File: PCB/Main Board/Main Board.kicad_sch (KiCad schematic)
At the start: 4 parts

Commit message: InAmp Progress
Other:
- sheet Current Amplifier ports: added ACC2.7k, ACC270, ACC27k, ACCen, InAmpx10, InAmpx3, InvAmpx10, InvAmp/2; removed x10, x3, x30/x100
- sheet Signal Source ports: added Bias, In; removed none
- sheet Voltage Amplifier ports: added ACC2.7k, ACC270, ACC27k, ACCen, InAmpx10, InAmpx3, InvAmpx10, InvAmp/2; removed x10, x3, x30/x100
- company: (none) -> Harry and Yuki - EEE3 Instrumentation
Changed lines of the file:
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@@
 	(generator_version "9.0")
 	(paper "A4")
+	(title_block
+		(date "2026-01-15")
+		(rev "Draft")
+		(company "Harry and Yuki - EEE3 Instrumentation")
+		(comment 1 "Work in Progress")
+	)
 	(text "LPOT\n"
 		(exclude_from_sim no)
@@
 	(wire
 		(pts
+			(xy 88.9 38.1) (xy 152.4 38.1)
+		)
+		(stroke
+			(width 0)
+			(type default)
+		)
+	)
+	(wire
+		(pts
 			(xy 177.8 111.76) (xy 190.5 111.76)
 		)
@@
 	(wire
 		(pts
+			(xy 88.9 35.56) (xy 152.4 35.56)
+		)
+		(stroke
+			(width 0)
+			(type default)
+		)
+	)
+	(wire
+		(pts
+			(xy 152.4 76.2) (xy 88.9 76.2)
+		)
+		(stroke
+			(width 0)
+			(type default)
+		)
+	)
+	(wire
+		(pts
 			(xy 215.9 114.3) (xy 228.6 114.3)
 		)
@@
 		(pts
 			(xy 222.25 63.5) (xy 228.6 63.5)
+		)
+		(stroke
+			(width 0)
+			(type default)
+		)
+	)
+	(wire
+		(pts
+			(xy 88.9 114.3) (xy 152.4 114.3)
 		)
 		(stroke
@@
 			)
 		)
+		(pin "Bias" input
+			(at 152.4 35.56 180)
+			(effects
+				(font
+					(size 1.27 1.27)
+				)
+				(justify left)
+			)
+		)
+		(pin "In" input
+			(at 152.4 38.1 180)
+			(effects
+				(font
+					(size 1.27 1.27)
+				)
+				(justify left)
+			)
+		)
 		(instances
 			(project "Main Board"
@@
 			)
 		)
-		(pin "x3" input
+		(pin "ACC2.7k" input
+			(at 152.4 66.04 180)
+			(effects
+				(font
+					(size 1.27 1.27)
+				)
+				(justify left)
+			)
+		)
+		(pin "ACC27k" input
+			(at 152.4 68.58 180)
+			(effects
+				(font
+					(size 1.27 1.27)
+				)
+				(justify left)
+			)
+		)
+		(pin "ACC270" input
+			(at 152.4 71.12 180)
+			(effects
+				(font
+					(size 1.27 1.27)
+				)
+				(justify left)
+			)
+		)
+		(pin "ACCen" input
+			(at 152.4 73.66 180)
+			(effects
+				(font
+					(size 1.27 1.27)
+				)
+				(justify left)
+			)
+		)
+		(pin "InAmpx3" input
+			(at 152.4 78.74 180)
+			(effects
+				(font
+					(size 1.27 1.27)
+				)
+				(justify left)
+			)
+		)
+		(pin "InAmpx10" input
 			(at 152.4 81.28 180)
 			(effects
@@
 			)
 		)
-		(pin "x10" input
+		(pin "InvAmpx10" input
+			(at 152.4 86.36 180)
+			(effects
+				(font
+					(size 1.27 1.27)
+				)
+				(justify left)
+			)
+		)
+		(pin "InvAmp{slash}2" input
 			(at 152.4 83.82 180)
-			(effects
-				(font
-					(size 1.27 1.27)
-				)
-				(justify left)
-			)
-		)
-		(pin "x30{slash}x100" input
-			(at 152.4 86.36 180)
 			(effects
 				(font
@@
 			)
 		)
-		(pin "x3" input
+		(pin "ACC2.7k" input
+			(at 152.4 104.14 180)
+			(effects
+				(font
+					(size 1.27 1.27)
+				)
+				(justify left)
+			)
+		)
+		(pin "ACC27k" input
+			(at 152.4 106.68 180)
+			(effects
+				(font
+					(size 1.27 1.27)
+				)
+				(justify left)
+			)
+		)
+		(pin "ACC270" input
+			(at 152.4 109.22 180)
+			(effects
+				(font
+					(size 1.27 1.27)
+				)
+				(justify left)
+			)
+		)
+		(pin "ACCen" input
+			(at 152.4 111.76 180)
+			(effects
+				(font
+					(size 1.27 1.27)
+				)
+				(justify left)
+			)
+		)
+		(pin "InAmpx3" input
+			(at 152.4 116.84 180)
+			(effects
+				(font
+					(size 1.27 1.27)
+				)
+				(justify left)
+			)
+		)
+		(pin "InAmpx10" input
 			(at 152.4 119.38 180)
 			(effects
@@
 			)
 		)
-		(pin "x10" input
+		(pin "InvAmpx10" input
+			(at 152.4 124.46 180)
+			(effects
+				(font
+					(size 1.27 1.27)
+				)
+				(justify left)
+			)
+		)
+		(pin "InvAmp{slash}2" input
 			(at 152.4 121.92 180)
 			(effects
 				(font
-					(size 1.27 1.27)
-				)
-				(justify left)
-			)
-		)
-		(pin "x30{slash}x100" input
-			(at 152.4 124.46 180)
-			(effects
-				(font

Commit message: ABB, InAmp
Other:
- note added: "Add reference"
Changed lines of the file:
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@@
+		)
+	)
+	(text "Add reference"
+		(exclude_from_sim no)
+		(at 116.84 135.89 0)
+		(effects
+			(font
+				(size 1.27 1.27)
+			)
+			(justify right top)
 		)
 	)
@@
 					(unit 1)
 				)
+			)
+		)
+	)
+	(symbol
+		(lib_id "power:+1V8")
+		(at 124.46 133.35 180)
+		(unit 1)
+		(exclude_from_sim no)
+		(in_bom yes)
+		(on_board yes)
+		(dnp no)
+		(fields_autoplaced yes)
+		(property "Reference" "#PWR0101"
+			(at 124.46 129.54 0)
+			(effects
+				(font
+					(size 1.27 1.27)
+				)
+				(hide yes)
+			)
+		)
+		(property "Value" "+1V8"
+			(at 124.46 138.43 0)
+			(effects
+				(font
+					(size 1.27 1.27)
+				)
+			)
+		)
+		(property "Footprint" ""
+			(at 124.46 133.35 0)
+			(effects
+				(font
+					(size 1.27 1.27)
+				)
+				(hide yes)
+			)
+		)
+		(property "Datasheet" ""
+			(at 124.46 133.35 0)
+			(effects
+				(font
+					(size 1.27 1.27)
+				)
+				(hide yes)
+			)
+		)
+		(property "Description" "Power symbol creates a global label with name \"+1V8\""
+			(at 124.46 133.35 0)
+			(effects
+				(font
+					(size 1.27 1.27)
+				)
+				(hide yes)
+			)
+		)
+		(pin "1"
+		)
+		(instances
+			(project "Main Board"
+				(path "/20aae4b7-3fb8-4924-82e8-1e7a29a313f8"
+					(reference "#PWR0101")
+					(unit 1)
+				)

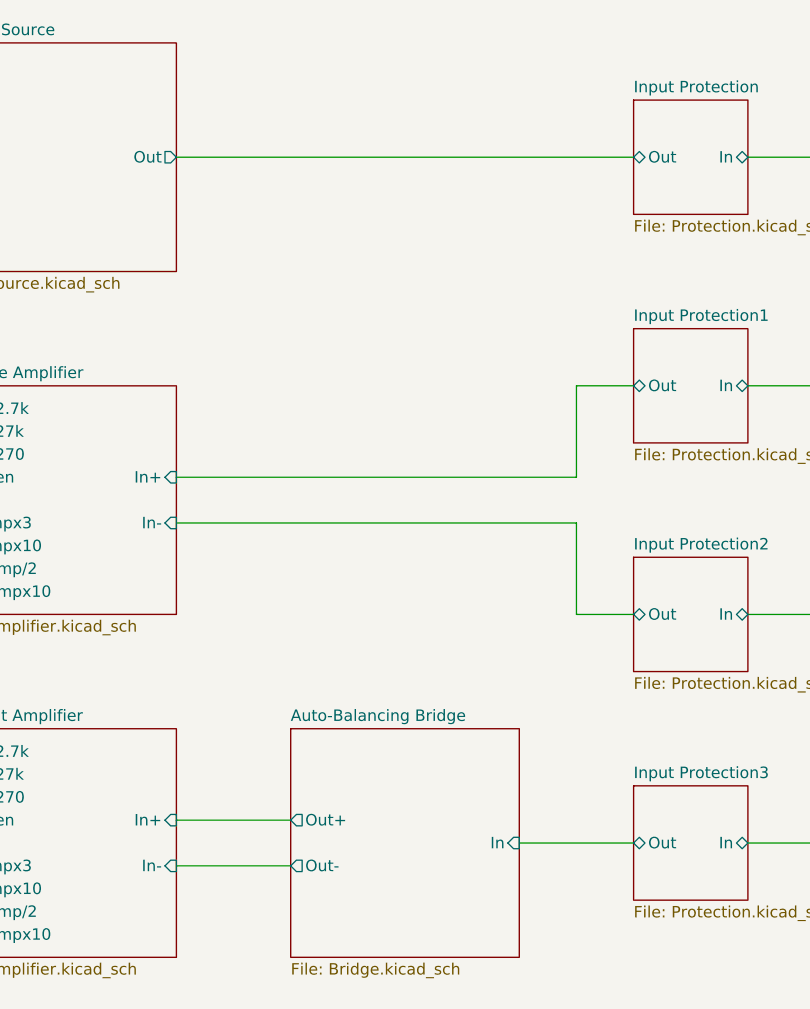
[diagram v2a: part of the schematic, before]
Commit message: Bias sense resistors
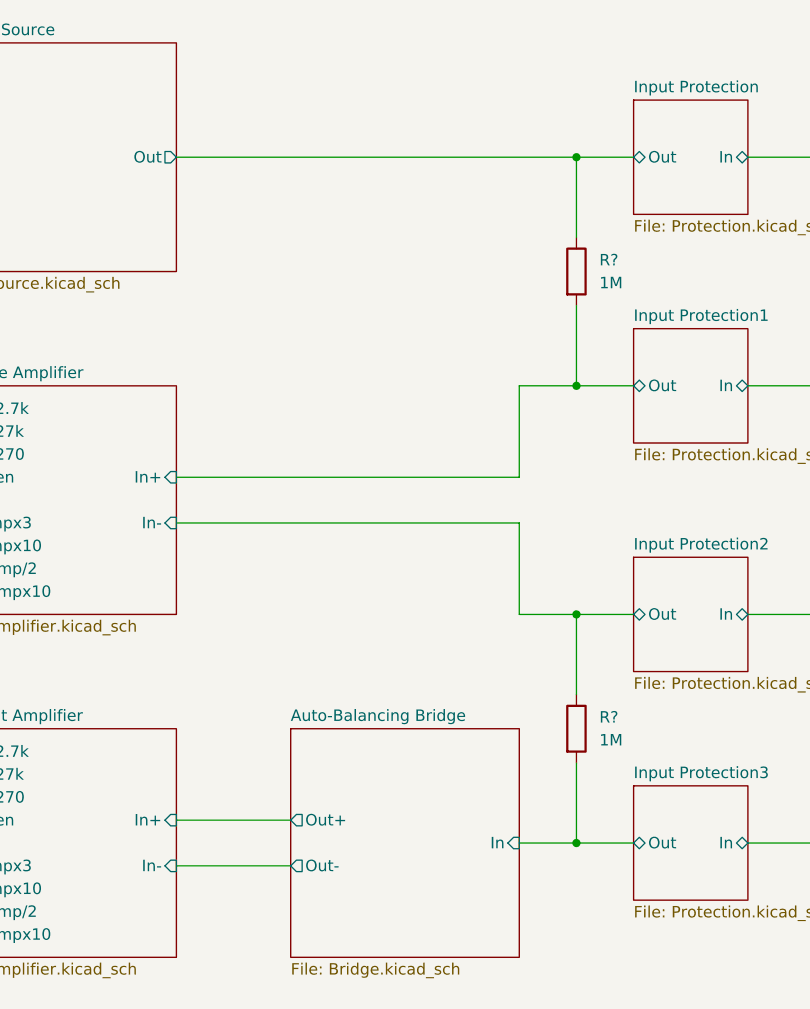
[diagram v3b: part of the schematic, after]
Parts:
- added R? (x2): 1M, symbol Device:R
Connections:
- net Auto-Balancing Bridge/In: now also R?.2
- net Input Protection/Out: now also R?.1
- net Input Protection1/Out: now also R?.2
- net Input Protection2/Out: now also R?.1
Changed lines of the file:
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@@
 		)
 	)
-	(wire
-		(pts
-			(xy 177.8 38.1) (xy 228.6 38.1)
-		)
-		(stroke
-			(width 0)
-			(type default)
-		)
-	)
-	(wire
-		(pts
-			(xy 222.25 73.66) (xy 222.25 63.5)
+	(junction
+		(at 222.25 38.1)
+		(diameter 0)
+		(color 0 0 0 0)
+	)
+	(junction
+		(at 222.25 114.3)
+		(diameter 0)
+		(color 0 0 0 0)
+	)
+	(junction
+		(at 222.25 88.9)
+		(diameter 0)
+		(color 0 0 0 0)
+	)
+	(junction
+		(at 222.25 63.5)
+		(diameter 0)
+		(color 0 0 0 0)
+	)
+	(wire
+		(pts
+			(xy 177.8 38.1) (xy 222.25 38.1)
+		)
+		(stroke
+			(width 0)
+			(type default)
+		)
+	)
+	(wire
+		(pts
+			(xy 215.9 73.66) (xy 215.9 63.5)
 		)
 		(stroke
@@
 	(wire
 		(pts
-			(xy 177.8 78.74) (xy 222.25 78.74)
+			(xy 222.25 88.9) (xy 222.25 97.79)
+		)
+		(stroke
+			(width 0)
+			(type default)
+		)
+	)
+	(wire
+		(pts
+			(xy 222.25 38.1) (xy 222.25 46.99)
+		)
+		(stroke
+			(width 0)
+			(type default)
+		)
+	)
+	(wire
+		(pts
+			(xy 177.8 78.74) (xy 215.9 78.74)
 		)
 		(stroke
@@
 	(wire
 		(pts
-			(xy 215.9 114.3) (xy 228.6 114.3)
-		)
-		(stroke
-			(width 0)
-			(type default)
-		)
-	)
-	(wire
-		(pts
-			(xy 222.25 78.74) (xy 222.25 88.9)
+			(xy 215.9 114.3) (xy 222.25 114.3)
+		)
+		(stroke
+			(width 0)
+			(type default)
+		)
+	)
+	(wire
+		(pts
+			(xy 215.9 78.74) (xy 215.9 88.9)
+		)
+		(stroke
+			(width 0)
+			(type default)
+		)
+	)
+	(wire
+		(pts
+			(xy 222.25 54.61) (xy 222.25 63.5)
 		)
 		(stroke
@@
 	(wire
 		(pts
+			(xy 215.9 88.9) (xy 222.25 88.9)
+		)
+		(stroke
+			(width 0)
+			(type default)
+		)
+	)
+	(wire
+		(pts
 			(xy 177.8 116.84) (xy 190.5 116.84)
 		)
@@
 	(wire
 		(pts
+			(xy 222.25 105.41) (xy 222.25 114.3)
+		)
+		(stroke
+			(width 0)
+			(type default)
+		)
+	)
+	(wire
+		(pts
+			(xy 222.25 114.3) (xy 228.6 114.3)
+		)
+		(stroke
+			(width 0)
+			(type default)
+		)
+	)
+	(wire
+		(pts
+			(xy 222.25 38.1) (xy 228.6 38.1)
+		)
+		(stroke
+			(width 0)
+			(type default)
+		)
+	)
+	(wire
+		(pts
+			(xy 215.9 63.5) (xy 222.25 63.5)
+		)
+		(stroke
+			(width 0)
+			(type default)
+		)
+	)
+	(wire
+		(pts
+			(xy 88.9 114.3) (xy 152.4 114.3)
+		)
+		(stroke
+			(width 0)
+			(type default)
+		)
+	)
+	(wire
+		(pts
+			(xy 241.3 88.9) (xy 248.92 88.9)
+		)
+		(stroke
+			(width 0)
+			(type default)
+		)
+	)
+	(wire
+		(pts
+			(xy 177.8 73.66) (xy 215.9 73.66)
+		)
+		(stroke
+			(width 0)
+			(type default)
+		)
+	)
+	(wire
+		(pts
 			(xy 222.25 63.5) (xy 228.6 63.5)
-		)
-		(stroke
-			(width 0)
-			(type default)
-		)
-	)
-	(wire
-		(pts
-			(xy 88.9 114.3) (xy 152.4 114.3)
-		)
-		(stroke
-			(width 0)
-			(type default)
-		)
-	)
-	(wire
-		(pts
-			(xy 241.3 88.9) (xy 248.92 88.9)
-		)
-		(stroke
-			(width 0)
-			(type default)
-		)
-	)
-	(wire
-		(pts
-			(xy 177.8 73.66) (xy 222.25 73.66)
 		)
 		(stroke
@@
 	)
 	(symbol
+		(lib_id "Device:R")
+		(at 222.25 101.6 0)
+		(unit 1)
+		(exclude_from_sim no)
+		(in_bom yes)
+		(on_board yes)
+		(dnp no)
+		(fields_autoplaced yes)
+		(property "Reference" "R?"
+			(at 224.79 100.3299 0)
+			(effects
+				(font
+					(size 1.27 1.27)
+				)
+				(justify left)
+			)
+		)
+		(property "Value" "1M"
+			(at 224.79 102.8699 0)
+			(effects
+				(font
+					(size 1.27 1.27)
+				)
+				(justify left)
+			)
+		)
+		(property "Footprint" ""
+			(at 220.472 101.6 90)
+			(effects
+				(font
+					(size 1.27 1.27)
+				)
+				(hide yes)
+			)
+		)
+		(property "Datasheet" "~"
+			(at 222.25 101.6 0)
+			(effects
+				(font
+					(size 1.27 1.27)
+				)
+				(hide yes)
+			)
+		)
+		(property "Description" "Resistor"
+			(at 222.25 101.6 0)
+			(effects
+				(font
+					(size 1.27 1.27)
+				)
+				(hide yes)
+			)
+		)
+		(pin "1"
+		)
+		(pin "2"
+		)
+		(instances
+			(project "Main Board"
+				(path "/20aae4b7-3fb8-4924-82e8-1e7a29a313f8"
+					(reference "R?")
+					(unit 1)
+				)
+			)
+		)
+	)
+	(symbol
 		(lib_id "power:+1V8")
 		(at 124.46 133.35 180)
@@
 					(unit 1)
 				)
+			)
+		)
+	)
+	(symbol
+		(lib_id "Device:R")
+		(at 222.25 50.8 0)
+		(unit 1)
+		(exclude_from_sim no)
+		(in_bom yes)
+		(on_board yes)
+		(dnp no)
+		(fields_autoplaced yes)
+		(property "Reference" "R?"
+			(at 224.79 49.5299 0)
+			(effects
+				(font
+					(size 1.27 1.27)
+				)
+				(justify left)
+			)
+		)
+		(property "Value" "1M"
+			(at 224.79 52.0699 0)
+			(effects
+				(font
+					(size 1.27 1.27)
+				)
+				(justify left)
+			)
+		)
+		(property "Footprint" ""
+			(at 220.472 50.8 90)
+			(effects
+				(font
+					(size 1.27 1.27)
+				)
+				(hide yes)
+			)
+		)
+		(property "Datasheet" "~"
+			(at 222.25 50.8 0)
+			(effects
+				(font
+					(size 1.27 1.27)
+				)
+				(hide yes)
+			)
+		)
+		(property "Description" "Resistor"
+			(at 222.25 50.8 0)
+			(effects
+				(font
+					(size 1.27 1.27)
+				)
+				(hide yes)
+			)
+		)
+		(pin "1"
+		)
+		(pin "2"
+		)
+		(instances
+			(project ""
+				(path "/20aae4b7-3fb8-4924-82e8-1e7a29a313f8"
+					(reference "R?")
+					(unit 1)
+				)

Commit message: Paniking further
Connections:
- net Guard_{out}: now reaches J?.2 (Ext)
- net Guard_{out}: now also J?.2 (Ext)
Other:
- added sheet Power (Power.kicad_sch)
- note removed: "Add reference"
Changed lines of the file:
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@@
-		)
-	)
-	(text "Add reference"
-		(exclude_from_sim no)
-		(at 116.84 135.89 0)
-		(effects
-			(font
-				(size 1.27 1.27)
-			)
-			(justify right top)
 		)
 	)
@@
 		)
 	)
+	(label "Guard_{out}"
+		(at 254 119.38 0)
+		(effects
+			(font
+				(size 1.27 1.27)
+			)
+			(justify left top)
+		)
+	)
+	(label "Guard_{out}"
+		(at 254 93.98 0)
+		(effects
+			(font
+				(size 1.27 1.27)
+			)
+			(justify left top)
+		)
+	)
 	(symbol
 		(lib_id "Connector:Conn_Coaxial")
@@
 	)
 	(symbol
-		(lib_id "power:+1V8")
-		(at 124.46 133.35 180)
-		(unit 1)
-		(exclude_from_sim no)
-		(in_bom yes)
-		(on_board yes)
-		(dnp no)
-		(fields_autoplaced yes)
-		(property "Reference" "#PWR0101"
-			(at 124.46 129.54 0)
-			(effects
-				(font
-					(size 1.27 1.27)
-				)
-				(hide yes)
-			)
-		)
-		(property "Value" "+1V8"
-			(at 124.46 138.43 0)
-			(effects
-				(font
-					(size 1.27 1.27)
-				)
-			)
-		)
-		(property "Footprint" ""
-			(at 124.46 133.35 0)
-			(effects
-				(font
-					(size 1.27 1.27)
-				)
-				(hide yes)
-			)
-		)
-		(property "Datasheet" ""
-			(at 124.46 133.35 0)
-			(effects
-				(font
-					(size 1.27 1.27)
-				)
-				(hide yes)
-			)
-		)
-		(property "Description" "Power symbol creates a global label with name \"+1V8\""
-			(at 124.46 133.35 0)
-			(effects
-				(font
-					(size 1.27 1.27)
-				)
-				(hide yes)
-			)
-		)
-		(pin "1"
-		)
-		(instances
-			(project "Main Board"
-				(path "/20aae4b7-3fb8-4924-82e8-1e7a29a313f8"
-					(reference "#PWR0101")
-					(unit 1)
-				)
-			)
-		)
-	)
-	(symbol
 		(lib_id "Connector:Conn_Coaxial")
 		(at 254 63.5 0)
@@
 			(project "Main Board"
 				(path "/20aae4b7-3fb8-4924-82e8-1e7a29a313f8"
-					(page "10")
+					(page "11")
+				)
+			)
+		)
+	)
+	(sheet
+		(at 63.5 139.7)
+		(size 25.4 25.4)
+		(exclude_from_sim no)
+		(in_bom yes)
+		(on_board yes)
+		(dnp no)
+		(fields_autoplaced yes)
+		(stroke
+			(width 0.1524)
+			(type solid)
+		)
+		(fill
+			(color 0 0 0 0.0000)
+		)
+		(property "Sheetname" "Power"
+			(at 63.5 138.9884 0)
+			(effects
+				(font
+					(size 1.27 1.27)
+				)
+				(justify left bottom)
+			)
+		)
+		(property "Sheetfile" "Power.kicad_sch"
+			(at 63.5 165.6846 0)
+			(effects
+				(font
+					(size 1.27 1.27)
+				)
+				(justify left top)
+			)
+		)
+		(instances
+			(project "Main Board"
+				(path "/20aae4b7-3fb8-4924-82e8-1e7a29a313f8"
+					(page "13")
 				)
 			)
@@
 			(project "Main Board"
 				(path "/20aae4b7-3fb8-4924-82e8-1e7a29a313f8"
-					(page "11")
+					(page "12")
 				)
 			)
@@
 			(project "Main Board"
 				(path "/20aae4b7-3fb8-4924-82e8-1e7a29a313f8"
-					(page "8")
+					(page "9")
 				)
 			)
@@
 			(project "Main Board"
 				(path "/20aae4b7-3fb8-4924-82e8-1e7a29a313f8"
-					(page "9")
-				)
-			)
+					(page "10")
+				)
+			)

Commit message: Signal
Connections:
- net Input Protection/Out is gone; now on net Signal Source/Out: R?.1
- net Input Protection1/Out is gone; now on net Voltage Amplifier/In+: R?.2
- net Input Protection2/Out is gone; now on net Voltage Amplifier/In-: R?.1
- net Input Protection3/In is gone; now on net Auto-Balancing Bridge/In: J?.1 (In)
- net Input Protection/In renamed Signal Source/Out
- net Input Protection1/In renamed Voltage Amplifier/In+
- net Input Protection2/In renamed Voltage Amplifier/In-
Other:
- removed sheet Input Protection
- removed sheet Input Protection1
- removed sheet Input Protection2
- removed sheet Input Protection3

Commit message: :anguished:
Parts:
- removed R? (x2): 1M, symbol Device:R
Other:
- sheet Signal Source ports: added x4, /10; removed none
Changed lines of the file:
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@@
-		)
-	)
-	(junction
-		(at 222.25 38.1)
-		(diameter 0)
-		(color 0 0 0 0)
-	)
-	(junction
-		(at 222.25 114.3)
-		(diameter 0)
-		(color 0 0 0 0)
-	)
-	(junction
-		(at 222.25 88.9)
-		(diameter 0)
-		(color 0 0 0 0)
-	)
-	(junction
-		(at 222.25 63.5)
-		(diameter 0)
-		(color 0 0 0 0)
-	)
-	(wire
-		(pts
-			(xy 177.8 38.1) (xy 222.25 38.1)
-		)
-		(stroke
-			(width 0)
-			(type default)
 		)
 	)
@@
 	(wire
 		(pts
-			(xy 222.25 88.9) (xy 222.25 97.79)
-		)
-		(stroke
-			(width 0)
-			(type default)
-		)
-	)
-	(wire
-		(pts
-			(xy 222.25 38.1) (xy 222.25 46.99)
-		)
-		(stroke
-			(width 0)
-			(type default)
-		)
-	)
-	(wire
-		(pts
 			(xy 177.8 78.74) (xy 215.9 78.74)
 		)
@@
 	(wire
 		(pts
-			(xy 222.25 88.9) (xy 248.92 88.9)
+			(xy 215.9 88.9) (xy 248.92 88.9)
 		)
 		(stroke
@@
 	(wire
 		(pts
-			(xy 215.9 114.3) (xy 222.25 114.3)
+			(xy 215.9 114.3) (xy 248.92 114.3)
 		)
 		(stroke
@@
 	(wire
 		(pts
-			(xy 222.25 54.61) (xy 222.25 63.5)
-		)
-		(stroke
-			(width 0)
-			(type default)
-		)
-	)
-	(wire
-		(pts
-			(xy 215.9 88.9) (xy 222.25 88.9)
+			(xy 88.9 45.72) (xy 152.4 45.72)
 		)
 		(stroke
@@
 	(wire
 		(pts
-			(xy 222.25 105.41) (xy 222.25 114.3)
-		)
-		(stroke
-			(width 0)
-			(type default)
-		)
-	)
-	(wire
-		(pts
-			(xy 222.25 114.3) (xy 248.92 114.3)
-		)
-		(stroke
-			(width 0)
-			(type default)
-		)
-	)
-	(wire
-		(pts
-			(xy 222.25 38.1) (xy 248.92 38.1)
-		)
-		(stroke
-			(width 0)
-			(type default)
-		)
-	)
-	(wire
-		(pts
-			(xy 215.9 63.5) (xy 222.25 63.5)
+			(xy 177.8 38.1) (xy 248.92 38.1)
 		)
 		(stroke
@@
 	(wire
 		(pts
-			(xy 222.25 63.5) (xy 248.92 63.5)
+			(xy 215.9 63.5) (xy 248.92 63.5)
+		)
+		(stroke
+			(width 0)
+			(type default)
+		)
+	)
+	(wire
+		(pts
+			(xy 88.9 48.26) (xy 152.4 48.26)
 		)
 		(stroke
@@
 	)
 	(symbol
-		(lib_id "Device:R")
-		(at 222.25 101.6 0)
-		(unit 1)
-		(exclude_from_sim no)
-		(in_bom yes)
-		(on_board yes)
-		(dnp no)
-		(fields_autoplaced yes)
-		(property "Reference" "R?"
-			(at 224.79 100.3299 0)
-			(effects
-				(font
-					(size 1.27 1.27)
-				)
-				(justify left)
-			)
-		)
-		(property "Value" "1M"
-			(at 224.79 102.8699 0)
-			(effects
-				(font
-					(size 1.27 1.27)
-				)
-				(justify left)
-			)
-		)
-		(property "Footprint" ""
-			(at 220.472 101.6 90)
-			(effects
-				(font
-					(size 1.27 1.27)
-				)
-				(hide yes)
-			)
-		)
-		(property "Datasheet" "~"
-			(at 222.25 101.6 0)
-			(effects
-				(font
-					(size 1.27 1.27)
-				)
-				(hide yes)
-			)
-		)
-		(property "Description" "Resistor"
-			(at 222.25 101.6 0)
-			(effects
-				(font
-					(size 1.27 1.27)
-				)
-				(hide yes)
-			)
-		)
-		(pin "1"
-		)
-		(pin "2"
-		)
-		(instances
-			(project "Main Board"
-				(path "/20aae4b7-3fb8-4924-82e8-1e7a29a313f8"
-					(reference "R?")
-					(unit 1)
-				)
-			)
-		)
-	)
-	(symbol
 		(lib_id "Connector:Conn_Coaxial")
 		(at 254 63.5 0)
@@
 				(path "/20aae4b7-3fb8-4924-82e8-1e7a29a313f8"
 					(reference "J?")
-					(unit 1)
-				)
-			)
-		)
-	)
-	(symbol
-		(lib_id "Device:R")
-		(at 222.25 50.8 0)
-		(unit 1)
-		(exclude_from_sim no)
-		(in_bom yes)
-		(on_board yes)
-		(dnp no)
-		(fields_autoplaced yes)
-		(property "Reference" "R?"
-			(at 224.79 49.5299 0)
-			(effects
-				(font
-					(size 1.27 1.27)
-				)
-				(justify left)
-			)
-		)
-		(property "Value" "1M"
-			(at 224.79 52.0699 0)
-			(effects
-				(font
-					(size 1.27 1.27)
-				)
-				(justify left)
-			)
-		)
-		(property "Footprint" ""
-			(at 220.472 50.8 90)
-			(effects
-				(font
-					(size 1.27 1.27)
-				)
-				(hide yes)
-			)
-		)
-		(property "Datasheet" "~"
-			(at 222.25 50.8 0)
-			(effects
-				(font
-					(size 1.27 1.27)
-				)
-				(hide yes)
-			)
-		)
-		(property "Description" "Resistor"
-			(at 222.25 50.8 0)
-			(effects
-				(font
-					(size 1.27 1.27)
-				)
-				(hide yes)
-			)
-		)
-		(pin "1"
-		)
-		(pin "2"
-		)
-		(instances
-			(project ""
-				(path "/20aae4b7-3fb8-4924-82e8-1e7a29a313f8"
-					(reference "R?")
 					(unit 1)
 				)
@@
 			(effects
 				(font
+					(size 1.27 1.27)
+				)
+				(justify left)
+			)
+		)
+		(pin "x4" input
+			(at 152.4 45.72 180)
+			(effects
+				(font
+					(size 1.27 1.27)
+				)
+				(justify left)
+			)
+		)
+		(pin "{slash}10" input
+			(at 152.4 48.26 180)
+			(effects
+				(font

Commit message: minor: pwr, stm, filters
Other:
- removed sheet Interface
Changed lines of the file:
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@@
-	)
-	(sheet
-		(at 25.4 25.4)
-		(size 25.4 165.1)
-		(exclude_from_sim no)
-		(in_bom yes)
-		(on_board yes)
-		(dnp no)
-		(fields_autoplaced yes)
-		(stroke
-			(width 0.1524)
-			(type solid)
-		)
-		(fill
-			(color 0 0 0 0.0000)
-		)
-		(property "Sheetname" "Interface"
-			(at 25.4 24.6884 0)
-			(effects
-				(font
-					(size 1.27 1.27)
-				)
-				(justify left bottom)
-			)
-		)
-		(property "Sheetfile" "Interface.kicad_sch"
-			(at 25.4 191.0846 0)
-			(effects
-				(font
-					(size 1.27 1.27)
-				)
-				(justify left top)
-			)
-		)
-		(instances
-			(project "Main Board"
-				(path "/20aae4b7-3fb8-4924-82e8-1e7a29a313f8"
-					(page "2")
-				)
-			)
-		)
 	)
 	(sheet
